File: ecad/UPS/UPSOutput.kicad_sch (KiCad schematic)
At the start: 18 parts, among them U2 MPQ5031GRE-0001-AEC1-P

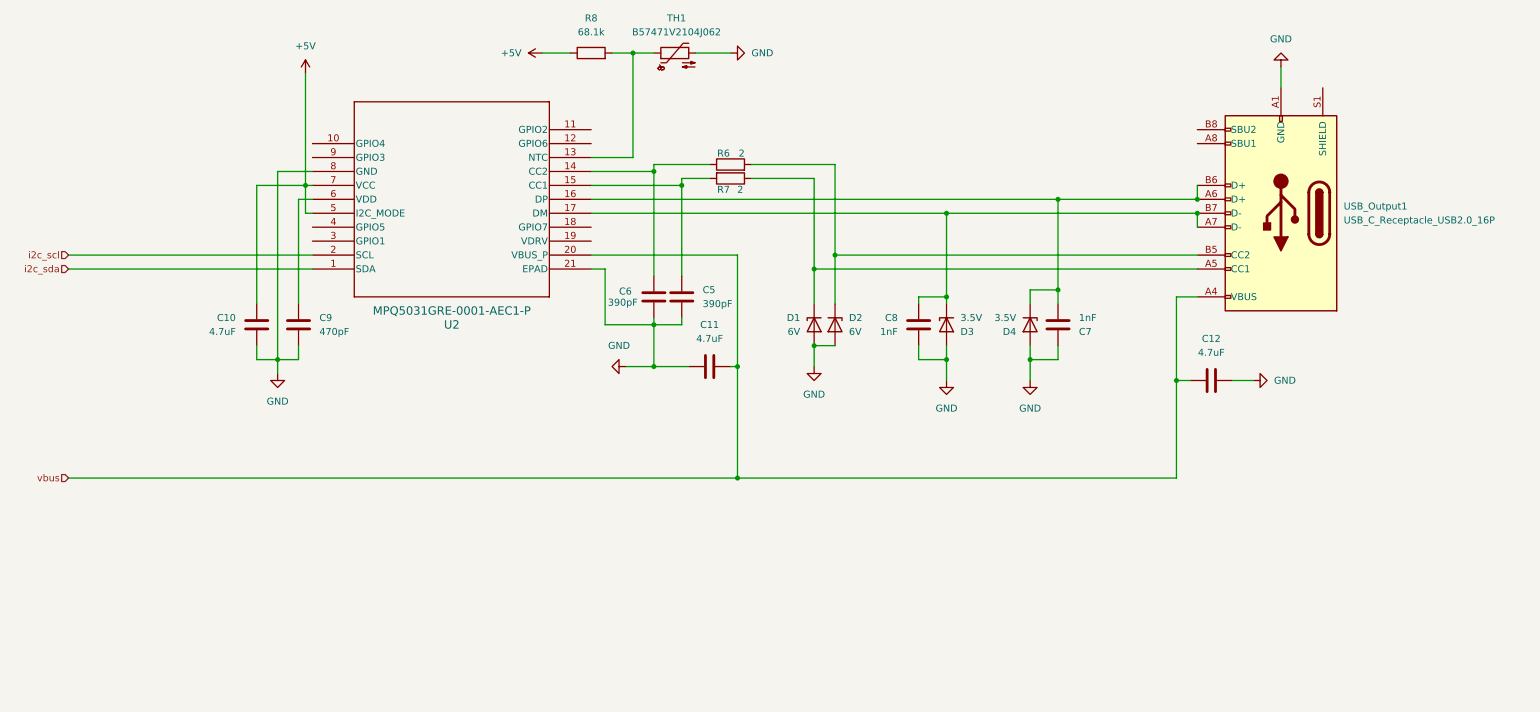
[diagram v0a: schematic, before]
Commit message: Did some routing, need to figure out how to route to BQ while appeasing DRC
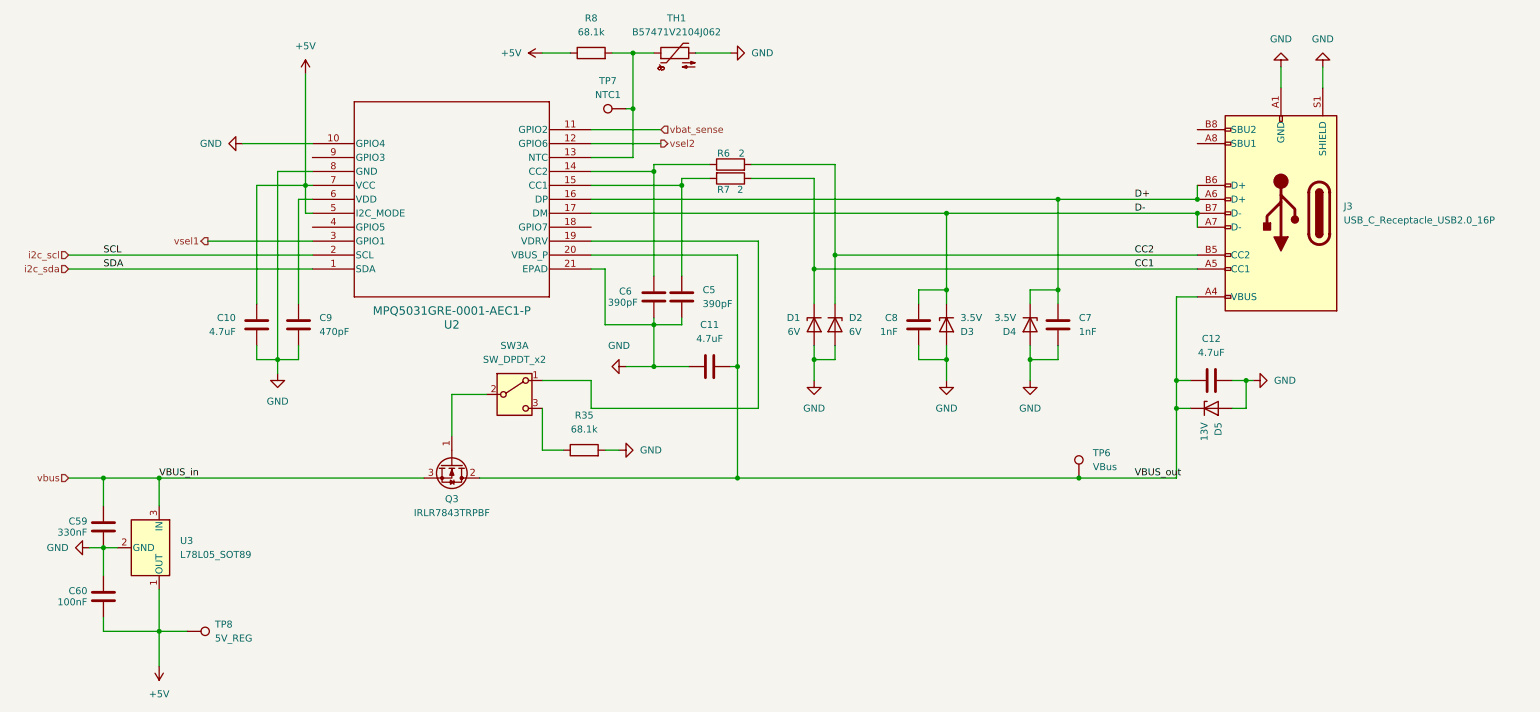
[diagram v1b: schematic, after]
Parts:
- added C59: 330nF, Capacitor_SMD:C_0603_1608Metric_Pad1.08x0.95mm_HandSolder, symbol Device:C
- added C60: 100nF, Capacitor_SMD:C_0805_2012Metric_Pad1.18x1.45mm_HandSolder, symbol Device:C
- added D5: 13V, Diode_SMD:D_SMB_Handsoldering, symbol Device:D_Zener
- added Q3: IRLR7843TRPBF, Package_TO_SOT_SMD:TO-252-2, symbol Transistor_FET:Q_NMOS_GDS
- added R35: 68.1k, Resistor_SMD:R_0805_2012Metric_Pad1.20x1.40mm_HandSolder, symbol Device:R
- added SW3: SW_DPDT_x2, UPS:SW_EG1218, symbol Switch:SW_DPDT_x2
- added TP6: VBus, TestPoint:TestPoint_Pad_D1.5mm, symbol Connector:TestPoint
- added TP7: NTC1, TestPoint:TestPoint_Pad_D1.5mm, symbol Connector:TestPoint
- added TP8: 5V_REG, TestPoint:TestPoint_Pad_D1.5mm, symbol Connector:TestPoint
- added U3: L78L05_SOT89, Package_TO_SOT_SMD:SOT-89-3, symbol Regulator_Linear:L78L05_SOT89
- C10, C11, C12: footprint (none) -> Capacitor_SMD:C_0805_2012Metric_Pad1.18x1.45mm_HandSolder
- C5, C6, C7, C8, C9: footprint (none) -> Capacitor_SMD:C_0603_1608Metric_Pad1.08x0.95mm_HandSolder
- D1, D2: footprint Diode_SMD:D_SMB-SMC_Universal_Handsoldering -> Diode_SMD:D_SMB_Handsoldering
- D3, D4: footprint UPS:SOD-962 SL2_TOS -> Diode_SMD:D_SMB_Handsoldering
- J3: renamed from USB_Output1; footprint (none) -> Connector_USB:USB_C_Receptacle_GCT_USB4110
- R6, R7: footprint (none) -> Resistor_SMD:R_1206_3216Metric_Pad1.30x1.75mm_HandSolder
- R8: footprint (none) -> Resistor_SMD:R_0805_2012Metric_Pad1.20x1.40mm_HandSolder
- U2: footprint QFN-20_MPQ5031_MNP -> UPS:QFN-20_MPQ5031_MNP
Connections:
- net +5V: now also C60.2, TP8.1, U3.1 (OUT)
- net GND: now also C7.2, J3.S1 (SHIELD), U2.10 (GPIO4), C59.2, C60.1, D5.2 (A), R35.2, U3.2 (GND); no longer C7.1
- net vbus: now also C59.1, Q3.3 (S), U3.3 (IN); no longer C11.2, C12.1, J3.A4 (VBUS), J3.A9 (VBUS), J3.B4 (VBUS), J3.B9 (VBUS), U2.20 (VBUS_P)
- net D+: now reaches D4.1 (K), J3.A6 (D+), J3.B6 (D+), U2.16 (DP)
- net D+: now also C7.1; no longer C7.2
- net CC1: now reaches D1.1 (K), J3.A5 (CC1), R7.1
- net D-: now reaches C8.1, D3.1 (K), J3.A7 (D-), J3.B7 (D-), U2.17 (DM)
- net CC2: now reaches D2.1 (K), J3.B5 (CC2), R6.2
- net vbat_sense: now reaches U2.11 (GPIO2)
- net vsel2: now reaches U2.12 (GPIO6)
- net at R8.2, TH1.1, U2.13 (NTC): now also TP7.1
- net at U2.19 (VDRV): now also SW3.1 (A)
- net vsel1: now reaches U2.3 (GPIO1)
- new net: Q3.1 (G), SW3.2 (B)
- new net: R35.1, SW3.3 (C)
- new net VBUS_out: C11.2, C12.1, D5.1 (K), J3.A4 (VBUS), J3.A9 (VBUS), J3.B4 (VBUS), J3.B9 (VBUS), Q3.2 (D), TP6.1, U2.20 (VBUS_P)
